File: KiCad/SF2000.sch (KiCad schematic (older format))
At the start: 71 parts, among them J1 Conn_2Rows-86Pins_even_odd, J2 Conn_01x02, J7 Conn_02x01, U1 LM1117-3.3, U19 74LVC1G57GV, U2 ABLIC S-1132B43-M5T1U, U3 TLV75533PDBVR, U4 SN74CBT16211, U5 SN74CBT16211, U6 SN74CBT3244PW, U7 SN74LVC16245ADGGR

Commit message: Add decoupling cap for pin 53,54 on RP2354A (U16)
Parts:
- C26: footprint Capacitor_SMD:C_0805_2012Metric_Pad1.15x1.40mm_HandSolder -> Capacitor_SMD:C_0603_1608Metric_Pad1.08x0.95mm_HandSolder
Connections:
- net 3V3: now also C26.2
- net GND: now also C26.1
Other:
- moved on the sheet: C26, C29
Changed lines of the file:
@@
 L Device:C C26
 U 1 1 62441B62
-P 8000 5450
-F 0 "C26" H 8050 5550 50  0000 L CNN
-F 1 "0.1uF" H 8000 5350 50  0000 L CNN
-F 2 "Capacitor_SMD:C_0805_2012Metric_Pad1.15x1.40mm_HandSolder" H 8038 5300 50  0001 C CNN
-F 3 "~" H 8000 5450 50  0001 C CNN
-	1    8000 5450
+P 3950 6150
+F 0 "C26" H 4000 6250 50  0000 L CNN
+F 1 "0.1uF" H 3950 6050 50  0000 L CNN
+F 2 "Capacitor_SMD:C_0603_1608Metric_Pad1.08x0.95mm_HandSolder" H 3988 6000 50  0001 C CNN
+F 3 "~" H 3950 6150 50  0001 C CNN
+	1    3950 6150
 	1    0    0    -1
 $EndComp
@@
 L Device:C C29
 U 1 1 6226157B
-P 4200 6150
-F 0 "C29" H 4250 6250 50  0000 L CNN
-F 1 "0.1uF" H 4200 6050 50  0000 L CNN
-F 2 "Capacitor_SMD:C_0805_2012Metric_Pad1.15x1.40mm_HandSolder" H 4238 6000 50  0001 C CNN
-F 3 "~" H 4200 6150 50  0001 C CNN
-	1    4200 6150
+P 6300 6150
+F 0 "C29" H 6350 6250 50  0000 L CNN
+F 1 "0.1uF" H 6300 6050 50  0000 L CNN
+F 2 "Capacitor_SMD:C_0805_2012Metric_Pad1.15x1.40mm_HandSolder" H 6338 6000 50  0001 C CNN
+F 3 "~" H 6300 6150 50  0001 C CNN
+	1    6300 6150
 	1    0    0    -1
 $EndComp
@@
 Connection ~ 2950 6000
 Connection ~ 2950 6300
-Connection ~ 3950 6000
-Connection ~ 3950 6300
 Wire Wire Line
 	4600 6800 4900 6800
@@
 Wire Wire Line
 	5450 6000 5700 6000
-Wire Wire Line
-	3950 6000 4200 6000
-Wire Wire Line
-	3950 6300 4200 6300
 Connection ~ 5450 6000
 Connection ~ 5700 6000
@@
 Text GLabel 7100 6300 0    50   Input ~ 0
 1V1
-Connection ~ 4200 6000
-Wire Wire Line
-	4200 6000 4450 6000
-Connection ~ 4200 6300
-Wire Wire Line
-	4200 6300 4450 6300
 Wire Wire Line
 	2950 6000 3200 6000
@@
 	7350 6300 8850 6300
 Connection ~ 3700 6000
+Connection ~ 3700 6300
 Wire Wire Line
 	3700 6000 3950 6000
-Connection ~ 3700 6300
 Wire Wire Line
 	3700 6300 3950 6300
+Connection ~ 3950 6000
+Connection ~ 3950 6300
+Wire Wire Line
+	6300 6000 6000 6000
+Wire Wire Line
+	3950 6000 4450 6000
+Wire Wire Line
+	3950 6300 4450 6300
+Connection ~ 6000 6000
+Wire Wire Line
+	6300 6300 6000 6300
+Connection ~ 6000 6300
 $EndSCHEMATC

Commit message: Add decoupling cap for pin 1 on RP2354A (U16)
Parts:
- C27: footprint Capacitor_SMD:C_0805_2012Metric_Pad1.15x1.40mm_HandSolder -> Capacitor_SMD:C_0603_1608Metric_Pad1.08x0.95mm_HandSolder
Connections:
- net 3V3: now also C27.2
- net GND: now also C27.1
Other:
- moved on the sheet: C27, C33
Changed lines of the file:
@@
 L Device:C C27
 U 1 1 62446240
-P 8250 5450
-F 0 "C27" H 8300 5550 50  0000 L CNN
-F 1 "0.1uF" H 8250 5350 50  0000 L CNN
-F 2 "Capacitor_SMD:C_0805_2012Metric_Pad1.15x1.40mm_HandSolder" H 8288 5300 50  0001 C CNN
-F 3 "~" H 8250 5450 50  0001 C CNN
-	1    8250 5450
+P 4200 6150
+F 0 "C27" H 4250 6250 50  0000 L CNN
+F 1 "0.1uF" H 4200 6050 50  0000 L CNN
+F 2 "Capacitor_SMD:C_0603_1608Metric_Pad1.08x0.95mm_HandSolder" H 4238 6000 50  0001 C CNN
+F 3 "~" H 4200 6150 50  0001 C CNN
+	1    4200 6150
 	1    0    0    -1
 $EndComp
@@
 L Device:C C33
 U 1 1 681A6453
-P 4450 6150
-F 0 "C33" H 4500 6250 50  0000 L CNN
-F 1 "0.1uF" H 4450 6050 50  0000 L CNN
-F 2 "Capacitor_SMD:C_0805_2012Metric_Pad1.18x1.45mm_HandSolder" H 4488 6000 50  0001 C CNN
-F 3 "~" H 4450 6150 50  0001 C CNN
-	1    4450 6150
+P 6600 6150
+F 0 "C33" H 6650 6250 50  0000 L CNN
+F 1 "0.1uF" H 6600 6050 50  0000 L CNN
+F 2 "Capacitor_SMD:C_0805_2012Metric_Pad1.18x1.45mm_HandSolder" H 6638 6000 50  0001 C CNN
+F 3 "~" H 6600 6150 50  0001 C CNN
+	1    6600 6150
 	1    0    0    -1
 $EndComp
@@
 	1    0    0    -1
 $EndComp
-Connection ~ 4450 6000
-Wire Wire Line
-	4450 6000 4700 6000
-Connection ~ 4450 6300
-Wire Wire Line
-	4450 6300 4700 6300
 Connection ~ 2950 6000
 Connection ~ 2950 6300
@@
 Wire Wire Line
 	6300 6000 6000 6000
-Wire Wire Line
-	3950 6000 4450 6000
-Wire Wire Line
-	3950 6300 4450 6300
 Connection ~ 6000 6000
 Wire Wire Line
 	6300 6300 6000 6300
 Connection ~ 6000 6300
+Wire Wire Line
+	6600 6000 6300 6000
+Wire Wire Line
+	3950 6000 4200 6000
+Wire Wire Line
+	3950 6300 4200 6300
+Connection ~ 6300 6000
+Wire Wire Line
+	6600 6300 6300 6300
+Connection ~ 6300 6300
+Connection ~ 4200 6000
+Wire Wire Line
+	4200 6000 4700 6000
+Connection ~ 4200 6300
+Wire Wire Line
+	4200 6300 4700 6300
 $EndSCHEMATC

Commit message: Add decoupling cap for pin 6 on RP2354A (U16)
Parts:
- C28: footprint Capacitor_SMD:C_0805_2012Metric_Pad1.15x1.40mm_HandSolder -> Capacitor_SMD:C_0603_1608Metric_Pad1.08x0.95mm_HandSolder
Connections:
- net 1V1: now also C28.2
- net 3V3: no longer C28.2
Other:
- moved on the sheet: C28, C35
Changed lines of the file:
@@
 L Device:C C35
 U 1 1 62559B16
-P 4700 6150
-F 0 "C35" H 4750 6250 50  0000 L CNN
-F 1 "0.1uF" H 4700 6050 50  0000 L CNN
-F 2 "Capacitor_SMD:C_0805_2012Metric_Pad1.15x1.40mm_HandSolder" H 4738 6000 50  0001 C CNN
-F 3 "~" H 4700 6150 50  0001 C CNN
-	1    4700 6150
-	1    0    0    -1
-$EndComp
-$Comp
-L Device:C C28
-U 1 1 6255AB6E
 P 6000 6150
-F 0 "C28" H 6050 6250 50  0000 L CNN
+F 0 "C35" H 6050 6250 50  0000 L CNN
 F 1 "0.1uF" H 6000 6050 50  0000 L CNN
 F 2 "Capacitor_SMD:C_0805_2012Metric_Pad1.15x1.40mm_HandSolder" H 6038 6000 50  0001 C CNN
 F 3 "~" H 6000 6150 50  0001 C CNN
 	1    6000 6150
+	1    0    0    -1
+$EndComp
+$Comp
+L Device:C C28
+U 1 1 6255AB6E
+P 7600 6150
+F 0 "C28" H 7650 6250 50  0000 L CNN
+F 1 "0.1uF" H 7600 6050 50  0000 L CNN
+F 2 "Capacitor_SMD:C_0603_1608Metric_Pad1.08x0.95mm_HandSolder" H 7638 6000 50  0001 C CNN
+F 3 "~" H 7600 6150 50  0001 C CNN
+	1    7600 6150
 	1    0    0    -1
 $EndComp
@@
 	1    0    0    -1
 $EndComp
-Connection ~ 4700 6000
-Connection ~ 4700 6300
 Wire Wire Line
 	2200 7100 2500 7100
@@
 Text GLabel 5450 5350 0    50   Input ~ 0
 GND
-Wire Wire Line
-	4700 6000 4950 6000
-Wire Wire Line
-	4700 6300 4950 6300
 Connection ~ 4950 6000
 Wire Wire Line
@@
 Connection ~ 7350 6000
 Wire Wire Line
-	7350 6000 8850 6000
+	7350 6000 7600 6000
 Connection ~ 7350 6300
 Wire Wire Line
-	7350 6300 8850 6300
+	7350 6300 7600 6300
 Connection ~ 3700 6000
 Connection ~ 3700 6300
@@
 Connection ~ 4200 6000
 Wire Wire Line
-	4200 6000 4700 6000
+	4200 6000 4450 6000
 Connection ~ 4200 6300
 Wire Wire Line
-	4200 6300 4700 6300
+	4200 6300 4450 6300
+Connection ~ 4450 6000
+Connection ~ 4450 6300
+Wire Wire Line
+	4450 6000 4950 6000
+Wire Wire Line
+	4450 6300 4950 6300
+Connection ~ 7600 6000
+Wire Wire Line
+	7600 6000 8850 6000
+Connection ~ 7600 6300
+Wire Wire Line
+	7600 6300 8850 6300
 $EndSCHEMATC

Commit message: Add UART0 two-pin-header for the RP2354A
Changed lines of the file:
@@
 Connection ~ 6300 6300
 Connection ~ 4200 6000
-Wire Wire Line
-	4200 6000 4450 6000
 Connection ~ 4200 6300
-Wire Wire Line
-	4200 6300 4450 6300
-Connection ~ 4450 6000
-Connection ~ 4450 6300
-Wire Wire Line
-	4450 6000 4950 6000
-Wire Wire Line
-	4450 6300 4950 6300
 Connection ~ 7600 6000
 Wire Wire Line
@@
 Wire Wire Line
 	7600 6300 8850 6300
+Wire Wire Line
+	4200 6000 4950 6000
+Wire Wire Line
+	4200 6300 4950 6300
 $EndSCHEMATC

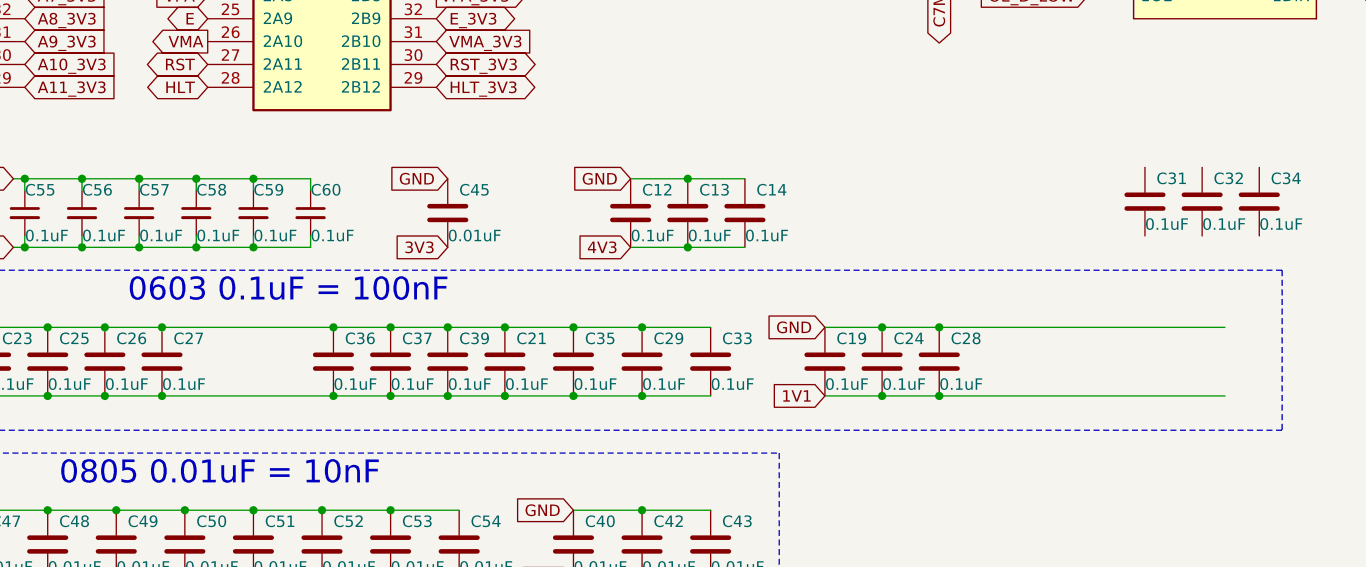
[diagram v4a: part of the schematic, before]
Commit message: Add decoupling caps for pin 31,42 on U7 (SN74LVC16245)
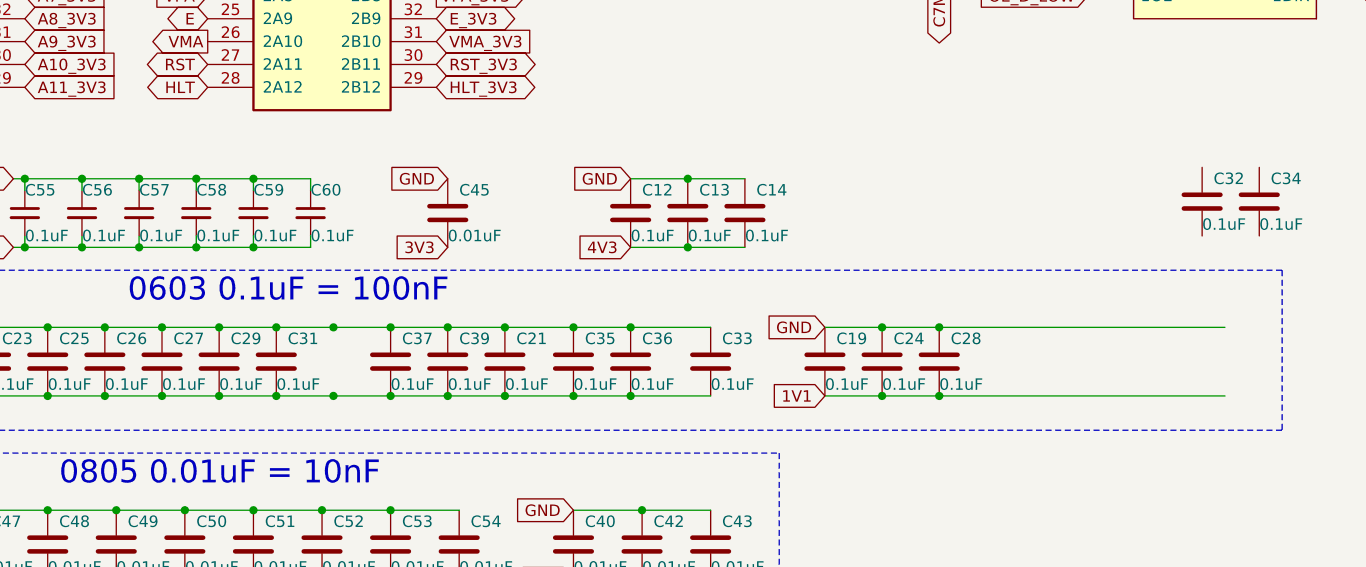
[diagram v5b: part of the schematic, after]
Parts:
- C29: footprint Capacitor_SMD:C_0805_2012Metric_Pad1.15x1.40mm_HandSolder -> Capacitor_SMD:C_0603_1608Metric_Pad1.08x0.95mm_HandSolder
- C31: footprint Capacitor_SMD:C_0805_2012Metric_Pad1.18x1.45mm_HandSolder -> Capacitor_SMD:C_0603_1608Metric_Pad1.08x0.95mm_HandSolder
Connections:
- net 3V3: now also C31.2
- net GND: now also C31.1
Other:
- moved on the sheet: C29, C31, C36
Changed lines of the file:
@@
 L Device:C C29
 U 1 1 6226157B
-P 6300 6150
-F 0 "C29" H 6350 6250 50  0000 L CNN
-F 1 "0.1uF" H 6300 6050 50  0000 L CNN
-F 2 "Capacitor_SMD:C_0805_2012Metric_Pad1.15x1.40mm_HandSolder" H 6338 6000 50  0001 C CNN
-F 3 "~" H 6300 6150 50  0001 C CNN
-	1    6300 6150
+P 4450 6150
+F 0 "C29" H 4500 6250 50  0000 L CNN
+F 1 "0.1uF" H 4450 6050 50  0000 L CNN
+F 2 "Capacitor_SMD:C_0603_1608Metric_Pad1.08x0.95mm_HandSolder" H 4488 6000 50  0001 C CNN
+F 3 "~" H 4450 6150 50  0001 C CNN
+	1    4450 6150
 	1    0    0    -1
 $EndComp
@@
 L Device:C C31
 U 1 1 681439C9
-P 8500 5450
-F 0 "C31" H 8550 5550 50  0000 L CNN
-F 1 "0.1uF" H 8500 5350 50  0000 L CNN
-F 2 "Capacitor_SMD:C_0805_2012Metric_Pad1.18x1.45mm_HandSolder" H 8538 5300 50  0001 C CNN
-F 3 "~" H 8500 5450 50  0001 C CNN
-	1    8500 5450
+P 4700 6150
+F 0 "C31" H 4750 6250 50  0000 L CNN
+F 1 "0.1uF" H 4700 6050 50  0000 L CNN
+F 2 "Capacitor_SMD:C_0603_1608Metric_Pad1.08x0.95mm_HandSolder" H 4738 6000 50  0001 C CNN
+F 3 "~" H 4700 6150 50  0001 C CNN
+	1    4700 6150
 	1    0    0    -1
 $EndComp
@@
 L Device:C C36
 U 1 1 623F86B0
-P 4950 6150
-F 0 "C36" H 5000 6250 50  0000 L CNN
-F 1 "0.1uF" H 4950 6050 50  0000 L CNN
-F 2 "Capacitor_SMD:C_0805_2012Metric_Pad1.15x1.40mm_HandSolder" H 4988 6000 50  0001 C CNN
-F 3 "~" H 4950 6150 50  0001 C CNN
-	1    4950 6150
+P 6250 6150
+F 0 "C36" H 6300 6250 50  0000 L CNN
+F 1 "0.1uF" H 6250 6050 50  0000 L CNN
+F 2 "Capacitor_SMD:C_0805_2012Metric_Pad1.15x1.40mm_HandSolder" H 6288 6000 50  0001 C CNN
+F 3 "~" H 6250 6150 50  0001 C CNN
+	1    6250 6150
 	1    0    0    -1
 $EndComp
@@
 Connection ~ 3950 6000
 Connection ~ 3950 6300
-Wire Wire Line
-	6300 6000 6000 6000
 Connection ~ 6000 6000
-Wire Wire Line
-	6300 6300 6000 6300
 Connection ~ 6000 6300
 Wire Wire Line
-	6600 6000 6300 6000
-Wire Wire Line
 	3950 6000 4200 6000
 Wire Wire Line
 	3950 6300 4200 6300
-Connection ~ 6300 6000
-Wire Wire Line
-	6600 6300 6300 6300
-Connection ~ 6300 6300
 Connection ~ 4200 6000
 Connection ~ 4200 6300
@@
 	7600 6300 8850 6300
 Wire Wire Line
-	4200 6000 4950 6000
-Wire Wire Line
-	4200 6300 4950 6300
+	4200 6000 4450 6000
+Wire Wire Line
+	4200 6300 4450 6300
+Connection ~ 4450 6000
+Wire Wire Line
+	4450 6000 4700 6000
+Connection ~ 4450 6300
+Wire Wire Line
+	4450 6300 4700 6300
+Wire Wire Line
+	6000 6000 6250 6000
+Wire Wire Line
+	6000 6300 6250 6300
+Connection ~ 6250 6000
+Wire Wire Line
+	6250 6000 6600 6000
+Connection ~ 6250 6300
+Wire Wire Line
+	6250 6300 6600 6300
+Connection ~ 4700 6000
+Wire Wire Line
+	4700 6000 4950 6000
+Connection ~ 4700 6300
+Wire Wire Line
+	4700 6300 4950 6300
 $EndSCHEMATC

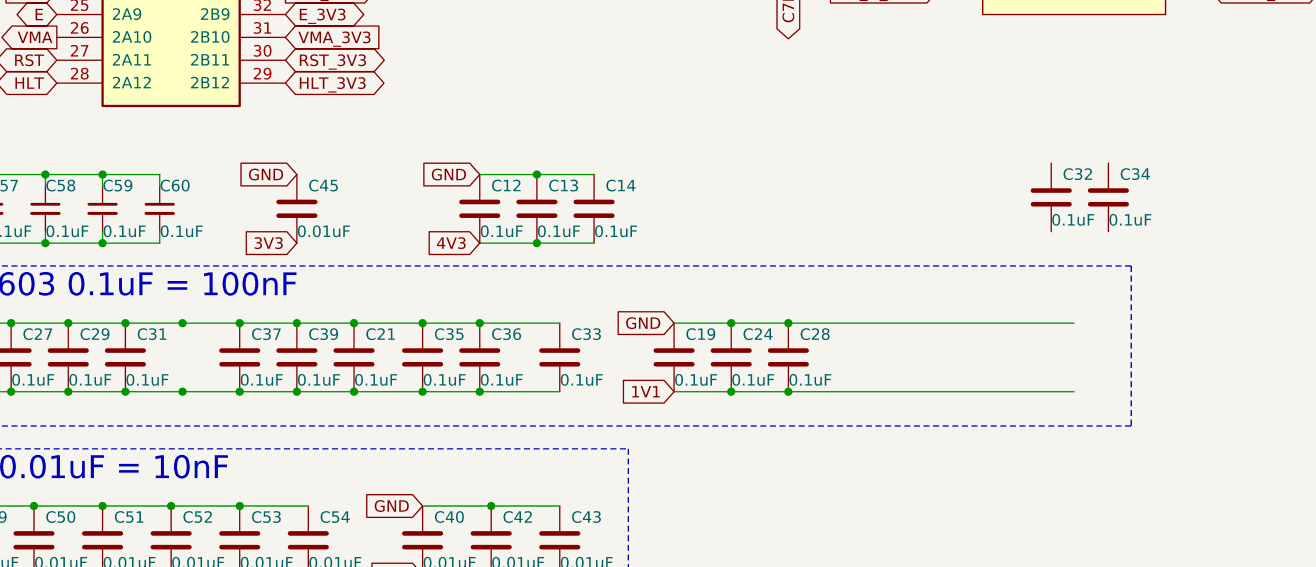
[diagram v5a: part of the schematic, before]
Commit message: Add decoupling caps for pin 7,18 on U7 (SN74LVC16245)
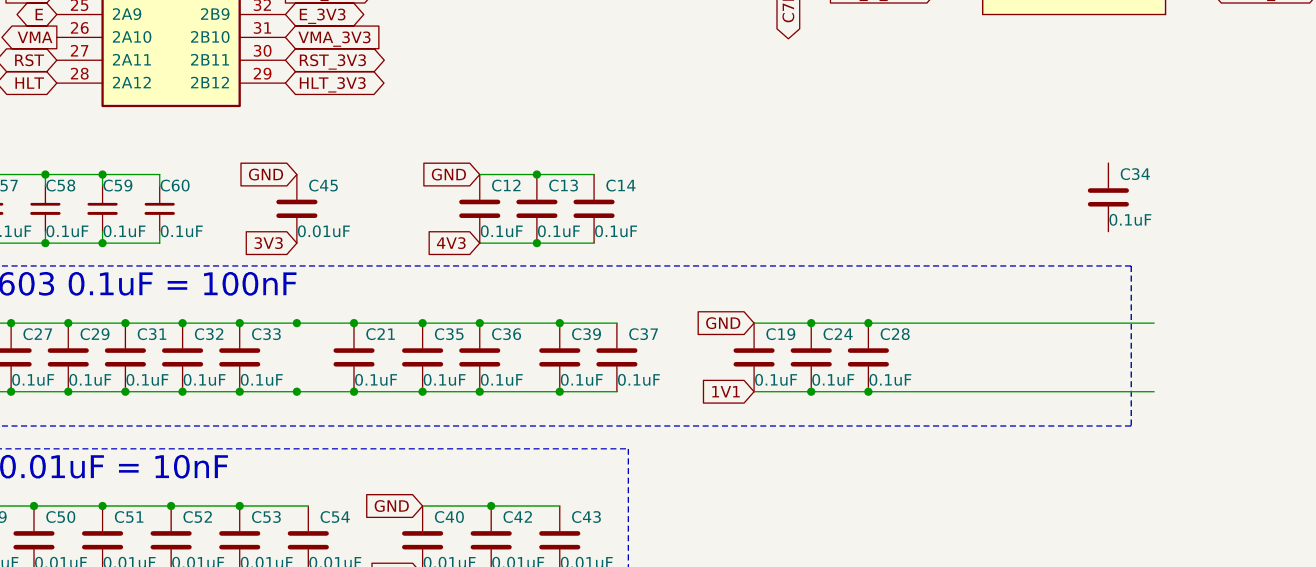
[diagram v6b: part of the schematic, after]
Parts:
- C32, C33: footprint Capacitor_SMD:C_0805_2012Metric_Pad1.18x1.45mm_HandSolder -> Capacitor_SMD:C_0603_1608Metric_Pad1.08x0.95mm_HandSolder
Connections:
- net 3V3: now also C32.2
- net GND: now also C32.1
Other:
- moved on the sheet: C19, C24, C28, C32, C33, C37, C39
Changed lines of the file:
@@
 L Device:C C19
 U 1 1 62524EDA
-P 7100 6150
-F 0 "C19" H 7150 6250 50  0000 L CNN
-F 1 "0.1uF" H 7100 6050 50  0000 L CNN
-F 2 "Capacitor_SMD:C_0603_1608Metric_Pad1.08x0.95mm_HandSolder" H 7138 6000 50  0001 C CNN
-F 3 "~" H 7100 6150 50  0001 C CNN
-	1    7100 6150
+P 7450 6150
+F 0 "C19" H 7500 6250 50  0000 L CNN
+F 1 "0.1uF" H 7450 6050 50  0000 L CNN
+F 2 "Capacitor_SMD:C_0603_1608Metric_Pad1.08x0.95mm_HandSolder" H 7488 6000 50  0001 C CNN
+F 3 "~" H 7450 6150 50  0001 C CNN
+	1    7450 6150
 	1    0    0    -1
 $EndComp
@@
 L Device:C C28
 U 1 1 6255AB6E
-P 7600 6150
-F 0 "C28" H 7650 6250 50  0000 L CNN
-F 1 "0.1uF" H 7600 6050 50  0000 L CNN
-F 2 "Capacitor_SMD:C_0603_1608Metric_Pad1.08x0.95mm_HandSolder" H 7638 6000 50  0001 C CNN
-F 3 "~" H 7600 6150 50  0001 C CNN
-	1    7600 6150
+P 7950 6150
+F 0 "C28" H 8000 6250 50  0000 L CNN
+F 1 "0.1uF" H 7950 6050 50  0000 L CNN
+F 2 "Capacitor_SMD:C_0603_1608Metric_Pad1.08x0.95mm_HandSolder" H 7988 6000 50  0001 C CNN
+F 3 "~" H 7950 6150 50  0001 C CNN
+	1    7950 6150
 	1    0    0    -1
 $EndComp
@@
 L Device:C C24
 U 1 1 6226DADA
-P 7350 6150
-F 0 "C24" H 7400 6250 50  0000 L CNN
-F 1 "0.1uF" H 7350 6050 50  0000 L CNN
-F 2 "Capacitor_SMD:C_0603_1608Metric_Pad1.08x0.95mm_HandSolder" H 7388 6000 50  0001 C CNN
-F 3 "~" H 7350 6150 50  0001 C CNN
-	1    7350 6150
+P 7700 6150
+F 0 "C24" H 7750 6250 50  0000 L CNN
+F 1 "0.1uF" H 7700 6050 50  0000 L CNN
+F 2 "Capacitor_SMD:C_0603_1608Metric_Pad1.08x0.95mm_HandSolder" H 7738 6000 50  0001 C CNN
+F 3 "~" H 7700 6150 50  0001 C CNN
+	1    7700 6150
 	1    0    0    -1
 $EndComp
@@
 L Device:C C39
 U 1 1 622B5AAE
-P 5450 6150
-F 0 "C39" H 5500 6250 50  0000 L CNN
-F 1 "0.1uF" H 5450 6050 50  0000 L CNN
-F 2 "Capacitor_SMD:C_0805_2012Metric_Pad1.15x1.40mm_HandSolder" H 5488 6000 50  0001 C CNN
-F 3 "~" H 5450 6150 50  0001 C CNN
-	1    5450 6150
+P 6600 6150
+F 0 "C39" H 6650 6250 50  0000 L CNN
+F 1 "0.1uF" H 6600 6050 50  0000 L CNN
+F 2 "Capacitor_SMD:C_0805_2012Metric_Pad1.15x1.40mm_HandSolder" H 6638 6000 50  0001 C CNN
+F 3 "~" H 6600 6150 50  0001 C CNN
+	1    6600 6150
 	1    0    0    -1
 $EndComp
@@
 L Device:C C33
 U 1 1 681A6453
-P 6600 6150
-F 0 "C33" H 6650 6250 50  0000 L CNN
-F 1 "0.1uF" H 6600 6050 50  0000 L CNN
-F 2 "Capacitor_SMD:C_0805_2012Metric_Pad1.18x1.45mm_HandSolder" H 6638 6000 50  0001 C CNN
-F 3 "~" H 6600 6150 50  0001 C CNN
-	1    6600 6150
+P 5200 6150
+F 0 "C33" H 5250 6250 50  0000 L CNN
+F 1 "0.1uF" H 5200 6050 50  0000 L CNN
+F 2 "Capacitor_SMD:C_0603_1608Metric_Pad1.08x0.95mm_HandSolder" H 5238 6000 50  0001 C CNN
+F 3 "~" H 5200 6150 50  0001 C CNN
+	1    5200 6150
 	1    0    0    -1
 $EndComp
@@
 L Device:C C32
 U 1 1 681E3D05
-P 8750 5450
-F 0 "C32" H 8800 5550 50  0000 L CNN
-F 1 "0.1uF" H 8750 5350 50  0000 L CNN
-F 2 "Capacitor_SMD:C_0805_2012Metric_Pad1.18x1.45mm_HandSolder" H 8788 5300 50  0001 C CNN
-F 3 "~" H 8750 5450 50  0001 C CNN
-	1    8750 5450
+P 4950 6150
+F 0 "C32" H 5000 6250 50  0000 L CNN
+F 1 "0.1uF" H 4950 6050 50  0000 L CNN
+F 2 "Capacitor_SMD:C_0603_1608Metric_Pad1.08x0.95mm_HandSolder" H 4988 6000 50  0001 C CNN
+F 3 "~" H 4950 6150 50  0001 C CNN
+	1    4950 6150
 	1    0    0    -1
 $EndComp
@@
 L Device:C C37
 U 1 1 623F7CFB
-P 5200 6150
-F 0 "C37" H 5250 6250 50  0000 L CNN
-F 1 "0.1uF" H 5200 6050 50  0000 L CNN
-F 2 "Capacitor_SMD:C_0805_2012Metric_Pad1.15x1.40mm_HandSolder" H 5238 6000 50  0001 C CNN
-F 3 "~" H 5200 6150 50  0001 C CNN
-	1    5200 6150
+P 6850 6150
+F 0 "C37" H 6900 6250 50  0000 L CNN
+F 1 "0.1uF" H 6850 6050 50  0000 L CNN
+F 2 "Capacitor_SMD:C_0805_2012Metric_Pad1.15x1.40mm_HandSolder" H 6888 6000 50  0001 C CNN
+F 3 "~" H 6850 6150 50  0001 C CNN
+	1    6850 6150
 	1    0    0    -1
 $EndComp
@@
 Text Notes 4050 5900 0    100  ~ 0
 0603 0.1uF = 100nF
-Text GLabel 7100 6000 0    50   Input ~ 0
+Text GLabel 7450 6000 0    50   Input ~ 0
 GND
 Wire Wire Line
@@
 Text GLabel 5450 5350 0    50   Input ~ 0
 GND
-Connection ~ 4950 6000
-Wire Wire Line
-	4950 6000 5200 6000
-Connection ~ 4950 6300
-Wire Wire Line
-	4950 6300 5200 6300
 Wire Wire Line
 	2500 6800 3100 6800
@@
 Wire Wire Line
 	2200 6300 2450 6300
-Wire Wire Line
-	5200 6000 5450 6000
-Connection ~ 5200 6000
-Wire Wire Line
-	5200 6300 5450 6300
-Connection ~ 5200 6300
 Connection ~ 2450 6000
 Wire Wire Line
@@
 	5700 6300 6000 6300
 Wire Wire Line
-	7100 6000 7350 6000
-Wire Wire Line
-	7100 6300 7350 6300
-Text GLabel 7100 6300 0    50   Input ~ 0
+	7450 6000 7700 6000
+Wire Wire Line
+	7450 6300 7700 6300
+Text GLabel 7450 6300 0    50   Input ~ 0
 1V1
 Wire Wire Line
@@
 Wire Wire Line
 	3450 6300 3700 6300
-Connection ~ 7350 6000
-Wire Wire Line
-	7350 6000 7600 6000
-Connection ~ 7350 6300
-Wire Wire Line
-	7350 6300 7600 6300
+Connection ~ 7700 6000
+Wire Wire Line
+	7700 6000 7950 6000
+Connection ~ 7700 6300
+Wire Wire Line
+	7700 6300 7950 6300
 Connection ~ 3700 6000
 Connection ~ 3700 6300
@@
 Connection ~ 4200 6000
 Connection ~ 4200 6300
-Connection ~ 7600 6000
-Wire Wire Line
-	7600 6000 8850 6000
-Connection ~ 7600 6300
-Wire Wire Line
-	7600 6300 8850 6300
+Connection ~ 7950 6000
+Wire Wire Line
+	7950 6000 9200 6000
+Connection ~ 7950 6300
+Wire Wire Line
+	7950 6300 9200 6300
 Wire Wire Line
 	4200 6000 4450 6000
@@
 	6250 6300 6600 6300
 Connection ~ 4700 6000
+Connection ~ 4700 6300
+Wire Wire Line
+	6850 6000 6600 6000
 Wire Wire Line
 	4700 6000 4950 6000
-Connection ~ 4700 6300
 Wire Wire Line
 	4700 6300 4950 6300
+Connection ~ 6600 6000
+Wire Wire Line
+	6850 6300 6600 6300
+Connection ~ 6600 6300
+Connection ~ 4950 6000
+Wire Wire Line
+	4950 6000 5200 6000
+Connection ~ 4950 6300
+Wire Wire Line
+	4950 6300 5200 6300
+Connection ~ 5200 6000
+Wire Wire Line
+	5200 6000 5450 6000
+Connection ~ 5200 6300
+Wire Wire Line
+	5200 6300 5450 6300
 $EndSCHEMATC
